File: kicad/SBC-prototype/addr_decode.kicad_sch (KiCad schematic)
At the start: 4 parts, among them U1 74HC00, U2 74HC00, U3 74HC00, U4 74HC00

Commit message: Started including hierarchical flow in the top level sheet
- First, hierarchical designs - I don't need a schematic to all fit on
  one sheet.
- I had the clock and reset lines as global labels, so I converted them
  to hierarchical labels instead, imported them on each sheet, and then
  connected the sheets together. It probably looks like overkill right
  now, but it will allow me to modify each block more easily
- The VIA has unconnected ports for now because I haven't wired them to
  anything on the prototyep in the lab yet. That's next, once the
  EEPROM, SRAM, and address decoders are all working (and VIA1 doesn't
  need a load except for maybe some resistors for now).
- Finally, the power rails and ground are global labels right now and
  aren't connected to anything on the top level design schematic. I'm
  not sure if that's normal, so for now I've just left them.
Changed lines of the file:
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@@
 	(title_block
 		(title "65C02 Single Board Computer")
-		(rev "Mk. 0")
+		(rev "Proto")
 	)
 	(junction
@@
 		)
 	)
-	(global_label "CLK"
-		(shape input)
-		(at 81.28 76.2 180)
-		(fields_autoplaced yes)
-		(effects
-			(font
-				(size 1.27 1.27)
-			)
-			(justify right)
-		)
-		(property "Intersheetrefs" "${INTERSHEET_REFS}"
-			(at 74.7267 76.2 0)
-			(effects
-				(font
-					(size 1.27 1.27)
-				)
-				(justify right)
-				(hide yes)
-			)
-		)
-	)
 	(hierarchical_label "ROM_OEB"
 		(shape output)
@@
 		)
 	)
+	(hierarchical_label "CLK"
+		(shape input)
+		(at 81.28 76.2 180)
+		(fields_autoplaced yes)
+		(effects
+			(font
+				(size 1.27 1.27)
+			)
+			(justify right)
+		)
+	)

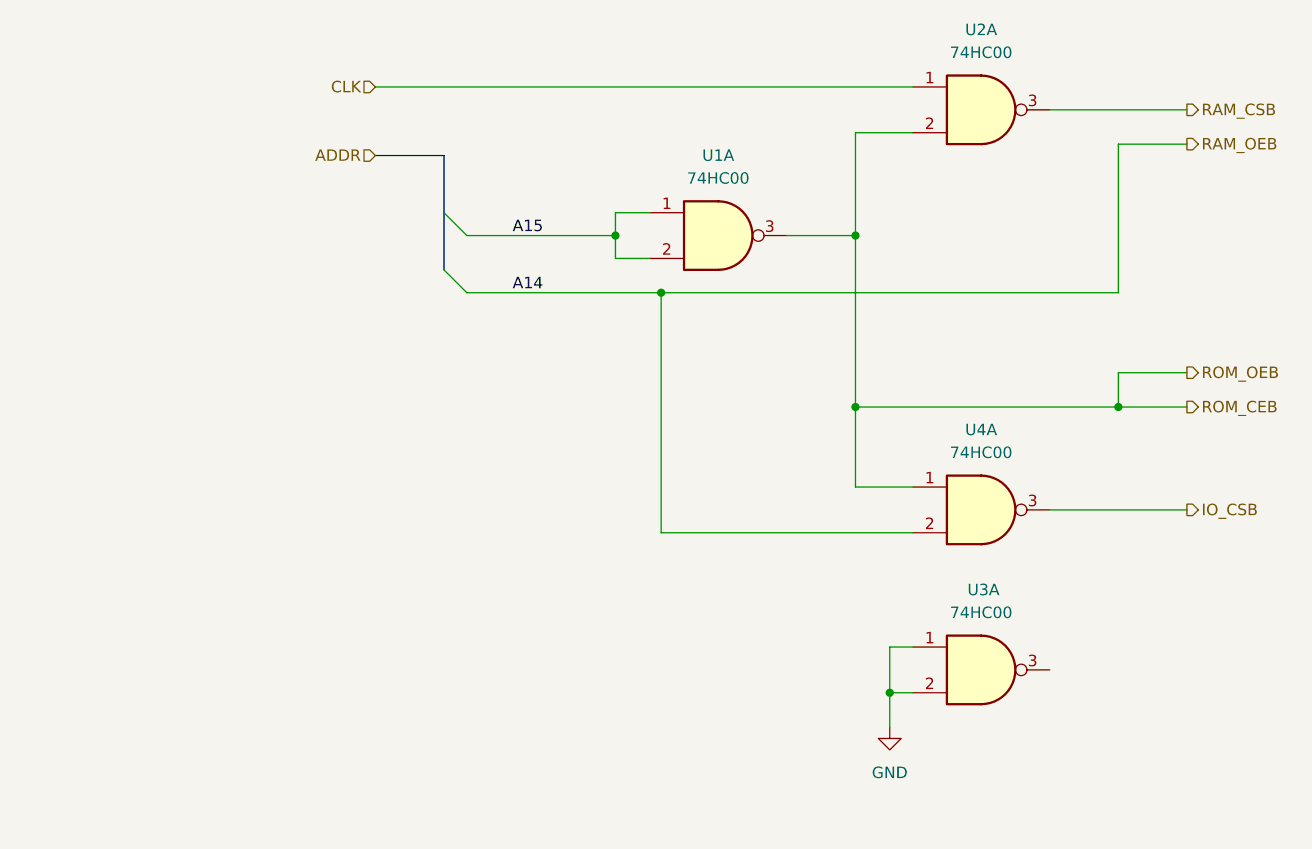
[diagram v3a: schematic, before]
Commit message: Fixed a ton of DRC errors and warnings
- VIA 1 is still unconnected since it's on the breadboard that way and I
  haven't hooked it to anything yet
- All the parts in the library have changed because I've modified my own
  versions of them. I'm not sure if I should add my changes to the
  library or find a way to tell the tool that it's OK that those are
  updated.
- The 74HC00 NAND gate was completely broken and would have been an
  interesting problem to sort out during routing and placement
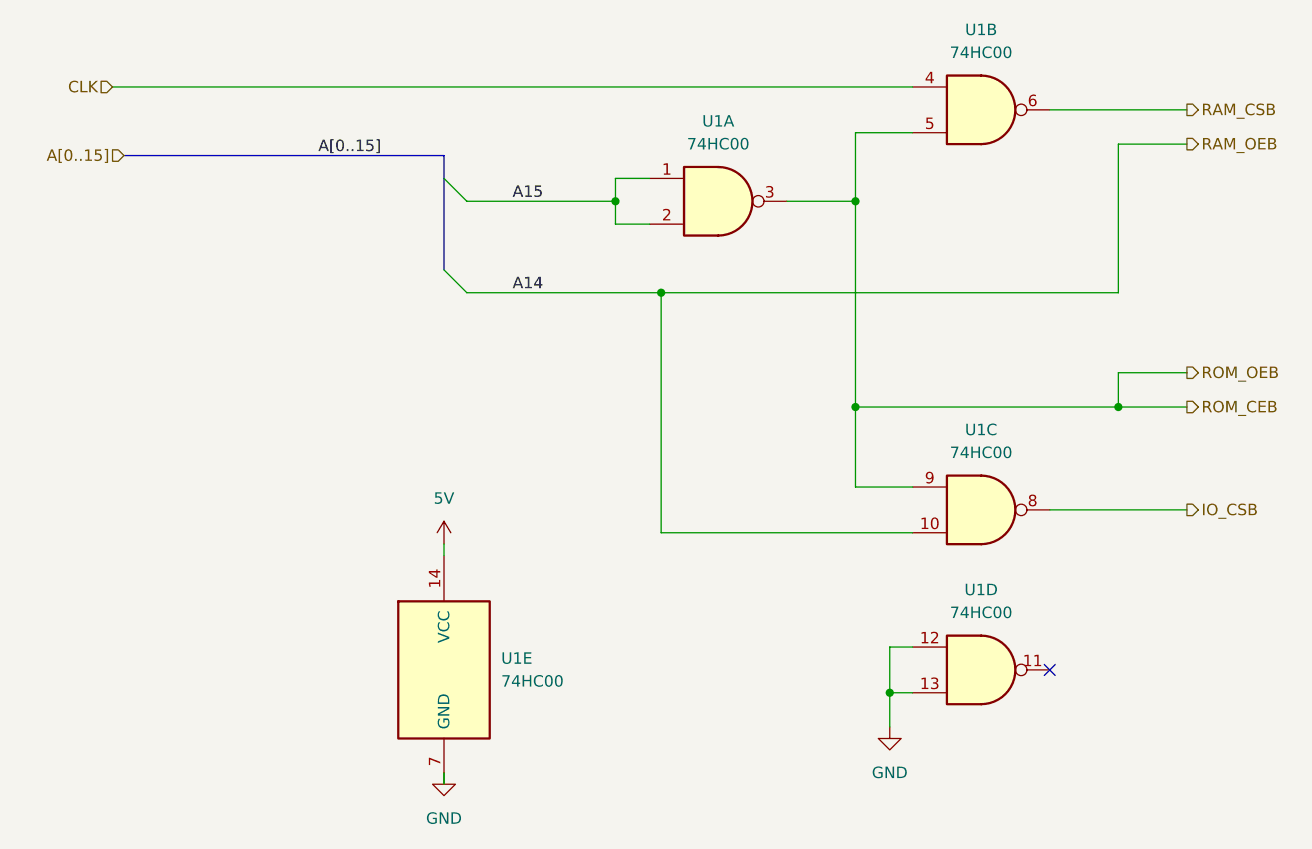
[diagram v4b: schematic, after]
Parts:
- removed U2, U3, U4: 74HC00, symbol 74xx:74HC00
- added unit 5 of U1
- added unit 3 of U1
- added unit 4 of U1
- added unit 2 of U1
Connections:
- net CLK: now also U1.4
- net GND: now also U1.12, U1.13, U1.7 (GND)
- net IO_CSB: now also U1.8
- net RAM_CSB: now also U1.6
- net RAM_OEB: now also U1.10
- net ROM_CEB: now also U1.5, U1.9
- new net 5V: U1.14 (VCC)
- no-connect marks 0 -> 1
